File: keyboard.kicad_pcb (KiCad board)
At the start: 2 copper layers, 140 parts, among them J1 CONN_02X04, J2 USB_A, J3 CONN_02X03, SW1 KEY_ESC, SW10 KEY_9, SW11 KEY_0, SW12 KEY_MINUS, SW13 KEY_EQUAL, SW14 KEY_DELETE, SW15 KEY_TAB, SW16 KEY_Q, SW17 KEY_W, SW18 KEY_E, SW19 KEY_R, SW2 KEY_1, SW20 KEY_T, SW21 KEY_Y, SW22 KEY_U, SW23 KEY_I, SW24 KEY_O, SW25 KEY_P, SW26 KEY_LBRACK, SW27 KEY_RBRACK, SW28 KEY_BACKSLH, SW29 KEY_CAPS, SW3 KEY_2, SW30 KEY_A, SW31 KEY_S, SW32 KEY_D, SW33 KEY_F, SW34 KEY_G, SW35 KEY_H, SW36 KEY_J, SW37 KEY_K, SW38 KEY_L, SW39 KEY_SEMI, SW4 KEY_3, SW40 KEY_APOS, SW41 KEY_ENTER, SW42 KEY_LSHIFT, SW43 KEY_Z, SW44 KEY_X, SW45 KEY_C, SW46 KEY_V, SW47 KEY_B, SW48 KEY_N, SW49 KEY_M, SW5 KEY_4, SW50 KEY_COMMA, SW51 KEY_PERIOD, SW52 KEY_SLASH, SW53 KEY_UP, SW54 KEY_RSHIFT, SW55 KEY_LCTRL, SW56 KEY_SPECIAL, SW57 KEY_LALT, SW58 KEY_SPACE, SW59 KEY_RALT, SW6 KEY_5, SW60 KEY_FN, SW61 KEY_RCTRL, SW62 KEY_LEFT, SW63 KEY_DOWN, SW64 KEY_RIGHT, SW7 KEY_6, SW8 KEY_7, SW9 KEY_8, U1 ATMEGA32U4-AU, Y1 16mhz

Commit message: More routing
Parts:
- J1: value CONN_02X04 -> CONN_01X05; footprint Pin_Headers:Pin_Header_Straight_2x04_Pitch2.54mm -> Pin_Headers:Pin_Header_Straight_1x05_Pitch2.54mm
- SW42: footprint cherrymx:CHERRY_PCB_200H -> cherrymx:CHERRY_PCB_225H
- SW54: footprint cherrymx:CHERRY_PCB_100H -> cherrymx:CHERRY_PCB_175H
- moved Y1 43.3 mm to (164.3, 239.8), turned to 90 degrees
- moved C2 42.9 mm to (157.7, 234.8), turned to 0 degrees
- moved C1 40.5 mm to (157.7, 238.1)
- moved R4 19.3 mm to (159.2, 248.7), turned to 180 degrees
- moved J3 11.7 mm to (215.1, 252.5)
- moved R3 5.08 mm to (88.1, 229.7)
- moved J1 1.27 mm to (135.1, 251.3)
- turned D57 to 270 degrees
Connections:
- J1 pad 1: VCC -> /EXT1
- J1 pad 2: /EXT1 -> /EXT2
- J1 pad 3: /EXT4 -> /EXT3
- J1 pad 4: /EXT2 -> GND
- J1 pad 5: /EXT5 -> VCC
- U1 pad 36: /EXT6 -> Net-(U1-Pad36)
- U1 pad 37: /EXT5 -> Net-(U1-Pad37)
- U1 pad 38: /EXT4 -> Net-(U1-Pad38)
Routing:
- net GND: track 212.7 -> 294.2 mm
- net VCC: track 198.1 -> 245.1 mm
- net Net-(R4-Pad1): track 0.00 -> 15.8 mm
- net /matrix/col3: track 67.6 -> 82.9 mm
- net (no net): track 0.00 -> 14.3 mm
- net /matrix/col6: track 176.7 -> 190.6 mm
- net /matrix/col7: track 67.6 -> 79.4 mm
- net /EXT1: track 0.00 -> 11.3 mm
- net Net-(C1-Pad2): track 33.9 -> 22.9 mm
- net /matrix/col8: track 156.9 -> 167.0 mm
- net /EXT2: track 0.00 -> 10.0 mm
- net Net-(D57-Pad2): track 0.00 -> 9.48 mm
- net /matrix/col9: track 67.1 -> 75.4 mm
- net Net-(C3-Pad1): track 0.00 -> 8.14 mm
- net /EXT3: track 3.28 -> 9.63 mm
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
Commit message: new net list
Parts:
- moved J3 11.4 mm to (211.0, 241.9)
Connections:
- U1 pad 18: /matrix/col6 -> /matrix/col4
- U1 pad 31: /matrix/col4 -> /matrix/col6
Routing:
- net /matrix/col4: track 66.3 -> 94.5 mm
- net (no net): track 14.3 -> 0.00 mm
- net /matrix/col6: track 190.6 -> 176.7 mm
- net GND: track 294.2 -> 286.8 mm

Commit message: checkpoint
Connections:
- D58 pad 1: /matrix/col4 -> /matrix/col6
- D59 pad 1: /matrix/col5 -> /matrix/col9
- D60 pad 1: /matrix/col6 -> /matrix/col10
- D61 pad 1: /matrix/col8 -> /matrix/col11
- D62 pad 1: /matrix/col11 -> /matrix/col12
- D63 pad 1: /matrix/col12 -> /matrix/col13
- D64 pad 1: /matrix/col13 -> /matrix/col14
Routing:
- net /matrix/col8: track 167.0 -> 77.7 mm
- net /matrix/col6: track 176.7 -> 91.9 mm
- net /matrix/col10: track 67.6 -> 102.3 mm
- net /matrix/col4: track 94.5 -> 66.4 mm
- net /matrix/col13: track 91.6 -> 118.9 mm
- net /matrix/col12: track 121.0 -> 102.3 mm
- net /matrix/col11: track 124.6 -> 107.4 mm
- net /matrix/col14: track 24.3 -> 31.5 mm

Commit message: route some cols
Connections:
- U1 pad 18: /matrix/col4 -> /matrix/col6
- U1 pad 31: /matrix/col6 -> /matrix/col4
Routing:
- net /matrix/col9: track 75.4 -> 158.8 mm
- net /matrix/col8: track 77.7 -> 142.1 mm
- net /matrix/col7: track 79.4 -> 134.2 mm
- net GND: track 286.8 -> 325.4 mm
- net /matrix/col6: track 91.9 -> 116.9 mm
- net VCC: track 245.1 -> 267.6 mm, vias 0 -> 4
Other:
- net class power: clearance 0.3 -> 0.25

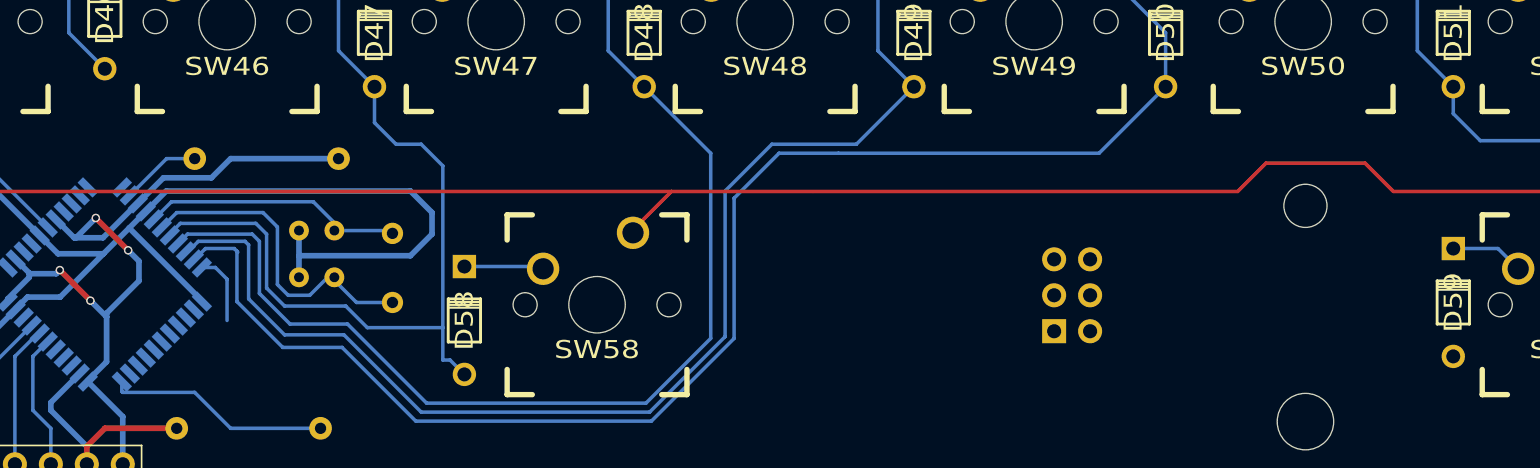
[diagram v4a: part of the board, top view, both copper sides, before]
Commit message: switch col 10 and 11
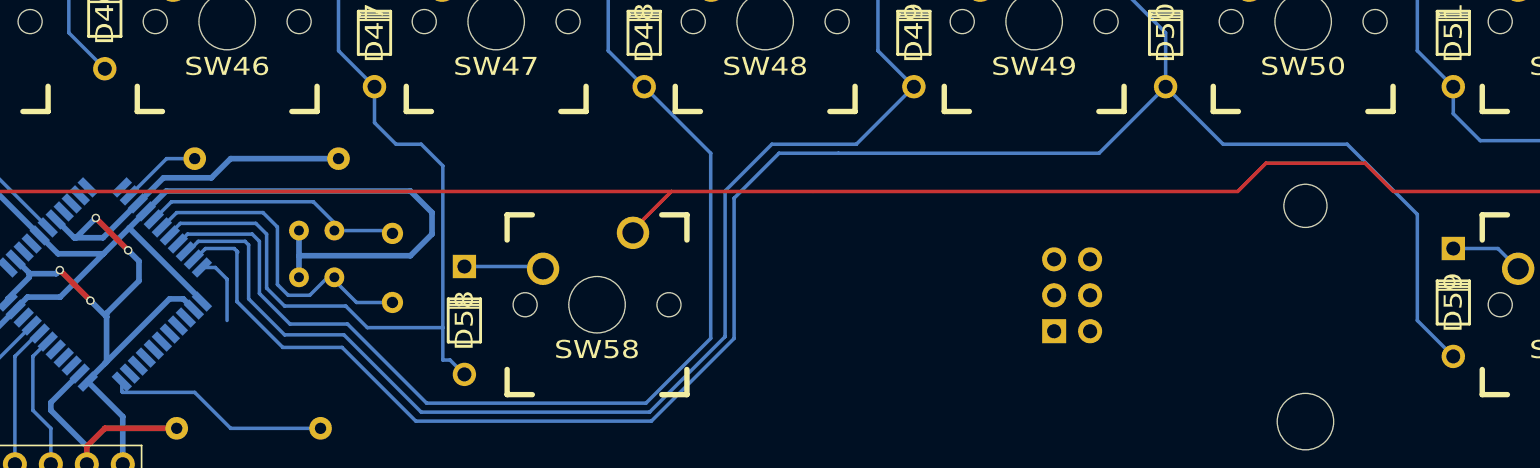
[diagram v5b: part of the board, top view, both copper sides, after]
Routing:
- net /matrix/col9: track 158.8 -> 191.4 mm
- net VCC: track 267.6 -> 276.1 mm
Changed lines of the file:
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@@
   (general
     (links 231)
-    (no_connects 27)
+    (no_connects 25)
     (area 43.149999 134.874999 333.431721 256.403333)
     (thickness 1.6)
     (drawings 1)
-    (tracks 702)
+    (tracks 711)
     (zones 0)
     (modules 140)
@@
   (segment (start 182.08 157.29) (end 186.645 157.29) (width 0.25) (layer B.Cu) (net 20))
   (segment (start 186.645 157.29) (end 186.815 157.46) (width 0.25) (layer B.Cu) (net 20))
+  (segment (start 218.91 224.6) (end 222.974 228.664) (width 0.25) (layer B.Cu) (net 21) (status 400000))
+  (segment (start 236.69 241.11) (end 239.23 243.65) (width 0.25) (layer B.Cu) (net 21) (status 800000))
+  (segment (start 236.69 233.617) (end 236.69 241.11) (width 0.25) (layer B.Cu) (net 21))
+  (segment (start 231.737 228.664) (end 236.69 233.617) (width 0.25) (layer B.Cu) (net 21))
+  (segment (start 222.974 228.664) (end 231.737 228.664) (width 0.25) (layer B.Cu) (net 21))
   (segment (start 195.796 229.299) (end 214.211 229.299) (width 0.25) (layer B.Cu) (net 21))
   (segment (start 153.3145 239.7765) (end 156.553 243.015) (width 0.25) (layer B.Cu) (net 21))
@@
   (segment (start 314.16 215.71) (end 318.065 215.71) (width 0.25) (layer B.Cu) (net 82))
   (segment (start 318.065 215.71) (end 319.815 217.46) (width 0.25) (layer B.Cu) (net 82))
+  (segment (start 143.98 244.158) (end 148.552 239.586) (width 0.4) (layer B.Cu) (net 83))
+  (segment (start 149.521483 239.586) (end 150.27325 240.337767) (width 0.4) (layer B.Cu) (net 83) (status 800000))
+  (segment (start 148.552 239.586) (end 149.521483 239.586) (width 0.4) (layer B.Cu) (net 83))
   (segment (start 144.107 240.856) (end 144.107 240.602) (width 0.4) (layer B.Cu) (net 83))
   (segment (start 141.948 235.268) (end 141.821 235.268) (width 0.4) (layer B.Cu) (net 83))
@@
   (segment (start 144.107 240.602) (end 146.393 238.316) (width 0.4) (layer B.Cu) (net 83))
   (segment (start 142.777918 245.428936) (end 142.777918 245.360082) (width 0.4) (layer B.Cu) (net 83) (status C00000))
-  (segment (start 142.777918 245.360082) (end 144.107 244.031) (width 0.4) (layer B.Cu) (net 83) (status 400000))
+  (segment (start 142.777918 245.360082) (end 143.98 244.158) (width 0.4) (layer B.Cu) (net 83) (status 400000))
+  (segment (start 143.98 244.158) (end 144.107 244.031) (width 0.4) (layer B.Cu) (net 83))
   (segment (start 140.551 237.808) (end 138.646 237.808) (width 0.4) (layer B.Cu) (net 83))
   (segment (start 140.805 237.554) (end 140.551 237.808) (width 0.4) (layer B.Cu) (net 83))

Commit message: more routing
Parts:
- moved R3 21.1 mm to (109.2, 229.7), turned to 180 degrees
- moved J2 3.25 mm to (54.6, 150.9)
- moved R2 3.05 mm to (114.0, 229.7)
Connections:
- U1 pad 22: /matrix/col11 -> /matrix/col10
- U1 pad 25: /matrix/col10 -> /matrix/col11
- U1 pad 32: /matrix/col5 -> /matrix/row1
- U1 pad 8: /matrix/row1 -> /matrix/col5
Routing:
- net /matrix/col13: track 118.9 -> 281.9 mm
- net /matrix/col12: track 102.3 -> 259.6 mm
- net Net-(J2-Pad3): track 0.00 -> 150.2 mm
- net Net-(J2-Pad2): track 0.00 -> 136.3 mm
- net /matrix/col11: track 107.4 -> 240.0 mm
- net /matrix/col10: track 102.3 -> 221.9 mm
- net Net-(R2-Pad2): track 0.00 -> 17.1 mm
- net /matrix/col5: track 66.3 -> 78.6 mm
- net GND: track 325.4 -> 326.7 mm
- net VCC: track 276.1 -> 277.1 mm

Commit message: almost done
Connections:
- U1 pad 1: /matrix/col14 -> /matrix/col3
- U1 pad 12: /matrix/col3 -> /matrix/col4
- U1 pad 29: /matrix/col1 -> /matrix/col14
- U1 pad 31: /matrix/col4 -> /matrix/col1
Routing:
- net /matrix/col14: track 31.5 -> 291.1 mm
- net /matrix/row5: track 327.2 -> 390.6 mm, vias 0 -> 1
- net /matrix/col3: track 82.9 -> 120.6 mm
- net Net-(R3-Pad1): track 0.00 -> 31.8 mm
- net /matrix/col13: track 281.9 -> 279.0 mm
